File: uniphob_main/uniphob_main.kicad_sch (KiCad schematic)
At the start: 116 parts, among them J1 USB_C_Receptacle, J2 Conn_01x06_Female, J3 Conn_01x02_Pin, J4 Rumble, J5 Conn_02x04_Counter_Clockwise, J6 Conn_01x06_Female, J7 Conn_01x05_Pin, P1 Endpoint, Q1 BSS138, Q2 BSS138, Q3 BSS138, Q4 Q_NMOS_GSD, Q5 Q_PMOS_GDS, Q6 Q_NMOS_GSD, SW1 GL18_SW, SW10 DPAD, SW11 DPAD, SW12 DPAD, SW2 GL18_SW, SW3 TS-1187A-B-A-B, SW5 BPAD, SW6 BPAD, SW7 BPAD, SW8 BPAD, SW9 DPAD, T1 36-8730, T2 36-8730, U1 ST_LSM6, U10 RP2040, U11 LP3986-33B3F, U2 ST_LSM6, U3 GH39F (Hall SOT23), U4 GH39F (Hall SOT23), U5 GH39F (Hall SOT23), U6 GH39F (Hall SOT23), U7 MCP3002, U8 MCP3002, U9 W25Q128JVS, Y1 Crystal_GND3

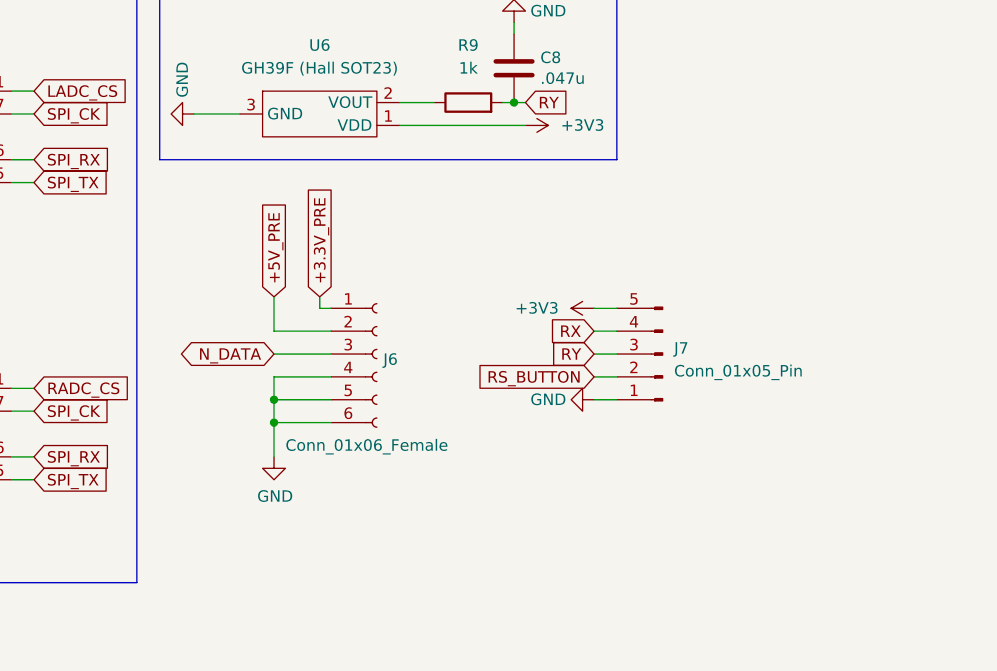
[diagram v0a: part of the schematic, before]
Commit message: Schematic updates
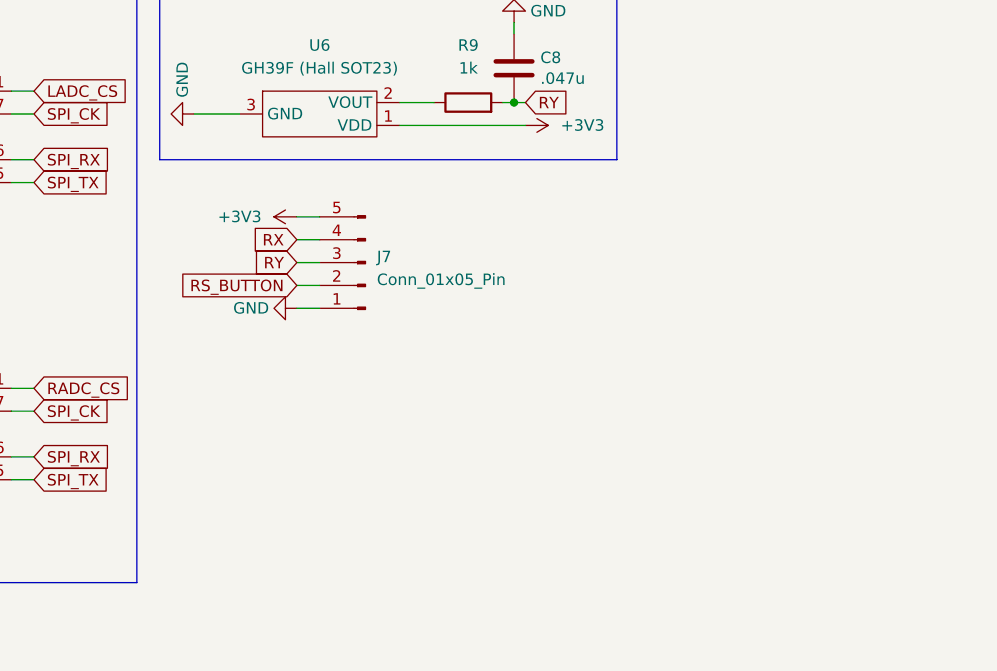
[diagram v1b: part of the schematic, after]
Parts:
- removed J6: Conn_01x06_Female, PhobGCC_2_0_0_footprints:GCC_Header_Straight_1x06_Pitch2.00mm, symbol Connector:Conn_01x06_Female
- D1, D2, D3, D4: footprint progcc_v3:SOT-363_SC-70-6 -> uniphob_footprints:SOT-363_SC-70-6
- J1: footprint progcc_v3:Shou Han Type-C 24P QCHT -> uniphob_footprints:Shou Han Type-C 24P QCHT
- J2: footprint progcc_v3:GCC_Header_Straight_1x06_Pitch2.00mm -> uniphob_footprints:GCC_Header_Straight_1x06_Pitch2.00mm
- J4: footprint progcc_v3:rumble_pins -> uniphob_footprints:rumble_pins
- J7: footprint (none) -> uniphob_footprints:molex_5034800540
- L1, L3, L5, L7: footprint progcc_v3:SK6805-EC-15 -> uniphob_footprints:SK6805-EC-15
- SW1, SW2: footprint progcc_v3:GL18 -> uniphob_footprints:GL18
- SW10, SW11, SW12, SW9: footprint progcc_v3:progcc_dpad -> (none)
- SW3: footprint progcc_v3:SW_TS-1187A-B-A-B -> uniphob_footprints:SW_TS-1187A-B-A-B
- SW5, SW6, SW7, SW8: footprint progcc_v3:progcc_bpad -> (none)
- T1, T2: footprint progcc_v3:KS_8730 -> (none)
- U1, U2: footprint progcc_v3:LGA14 -> uniphob_footprints:LGA14
- U3, U4, U5, U6: footprint progcc_v3:GH39F -> uniphob_footprints:GH39F
- U7, U8: footprint progcc_v3:SOIC-8_3.9x4.9mm_P1.27mm -> uniphob_footprints:SOIC-8_3.9x4.9mm_P1.27mm
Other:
- moved on the sheet: J7

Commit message: Checkpoint
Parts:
- removed SW6, SW7: BPAD, symbol Switch:SW_Push
- removed T1, T2: 36-8730, symbol Connector:TestPoint
- added C20, C21: 100n, Capacitor_SMD:C_0402_1005Metric, symbol Device:C
- added J6, J8: Conn_01x02_Socket, Connector_PinSocket_2.00mm:PinSocket_1x02_P2.00mm_Vertical, symbol Connector:Conn_01x02_Socket
- added RV1, RV2: Slider_GCC-Gamecube_MB, uniphob_footprints:GCC_Slider, symbol uniphob_symbols:Slider_GCC-Gamecube_MB
- J5: footprint (none) -> Connector_PinSocket_2.00mm:PinSocket_2x04_P2.00mm_Vertical
- SW10, SW11, SW12, SW9: footprint (none) -> uniphob_footprints:Dpad_Contact_TL3315NF_2_gba
- SW5, SW8: footprint (none) -> uniphob_footprints:Z_Switch_Edge_Omron
- SW5, SW6, SW7, SW8: footprint (none) -> uniphob_footprints:ABXY_Contact_Omron_Switch_Circley
- SW5: footprint (none) -> uniphob_footprints:Start_Contact
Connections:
- net +3V3: now also RV1.1 (V+), RV2.1 (V+)
- net GND: now also C20.2, C21.2, RV1.2 (GND), RV2.2 (GND)
- net L_ANALOG: now also C20.1, RV1.3 (Signal)
- net L_Pull: now also J8.2 (Pin_2)
- net R_ANALOG: now also C21.1, RV2.3 (Signal)
- net R_Pull: now also J6.2 (Pin_2)
- net Scan_C: now also J6.1 (Pin_1), J8.1 (Pin_1)

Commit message: ROUTING
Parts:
- removed C7, C8: .047u, Capacitor_SMD:C_0603_1608Metric_Pad1.08x0.95mm_HandSolder, symbol Device:C
- removed J1: USB_C_Receptacle, uniphob_footprints:Shou Han Type-C 24P QCHT, symbol Connector:USB_C_Receptacle
- removed R8, R9: 1k, Resistor_SMD:R_0402_1005Metric, symbol Device:R
- removed SW2: GL18_SW, uniphob_footprints:GL18, symbol progcc_v3:GL18_SW
- removed TP1, TP10, TP11, TP12, TP13, TP14, TP15, TP16, TP2, TP6, TP8, TP9: TestPoint, TestPoint:TestPoint_Pad_D1.5mm, symbol Connector:TestPoint
- removed U5, U6: GH39F (Hall SOT23), uniphob_footprints:GH39F, symbol progcc_v3:GH39F (Hall SOT23)
- added J1: USB4105-GF-A-060, uniphob_footprints:GCT_USB4105-GF-A-060, symbol uniphob_symbols:USB4105-GF-A-060
- added R25, R26: 5.1k, Resistor_SMD:R_0603_1608Metric_Pad0.98x0.95mm_HandSolder, symbol Device:R
- J5: footprint Connector_PinSocket_2.00mm:PinSocket_2x04_P2.00mm_Vertical -> uniphob_footprints:PinSocket_2x05_P2.00mm_Vertical; symbol Connector_Generic:Conn_02x04_Counter_Clockwise -> Connector_Generic:Conn_02x05_Counter_Clockwise
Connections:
- net +3.3V_PRE: now also J5.8 (Pin_8); no longer J5.6 (Pin_6)
- net +5V_PRE: now also J5.7 (Pin_7), J1.A4_B9 (VBUS), J1.B4_A9 (VBUS); no longer J5.5 (Pin_5)
- net CC1: now also J5.5 (Pin_5), R25.1; no longer R1.1
- net CC2: now also J5.6 (Pin_6), R26.2; no longer R2.1
- net D+: now also J5.10 (Pin_10), J1.A6 (DP1), J1.B6 (DP2); no longer J5.8 (Pin_8)
- net D-: now also J5.9 (Pin_9), J1.A7 (DN1), J1.B7 (DN2); no longer J5.7 (Pin_7)
- net GND: now also J1.A1_B12 (GND), J1.B1_A12 (GND), J1.S1 (SHELL_GND), J1.S2 (SHELL_GND), J1.S3 (SHELL_GND), J1.S4 (SHELL_GND), R25.2, R26.1
- new net: J1.A5 (CC1), R1.1
- new net: J1.B5 (CC2), R2.1
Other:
- note removed: "USB Port"

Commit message: Routing done
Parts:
- added J9: Conn_01x05_Pin, Connector_PinHeader_2.00mm:PinHeader_1x05_P2.00mm_Vertical, symbol Connector:Conn_01x05_Pin
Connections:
- net +3V3: now also J9.5 (Pin_5)
- net GND: now also J9.1 (Pin_1)
- net RS_BUTTON: now also J9.2 (Pin_2)
- net RX: now also J9.4 (Pin_4)
- net RY: now also J9.3 (Pin_3)
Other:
- note added: "To Sub-Stick PCB"
- moved on the sheet: J7
